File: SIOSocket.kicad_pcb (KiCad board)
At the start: 2 copper layers, 46 x 26 mm, 3 parts, among them J1 Atari_SIO_Connector, J2 Conn_2Rows-13Pins

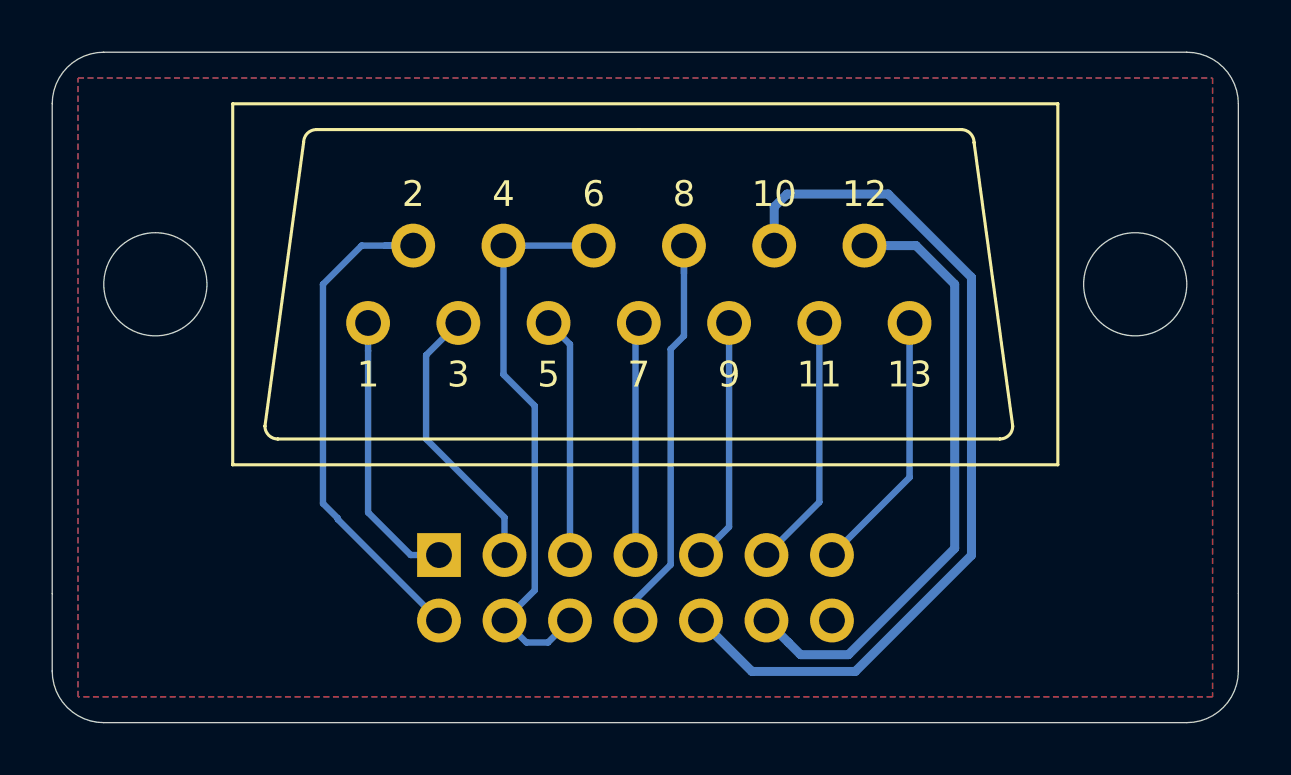
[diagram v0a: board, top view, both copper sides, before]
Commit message: Upgrade to KiCad 5.1 and changes to 3D printed SIO port for Atari800XL PCB Project
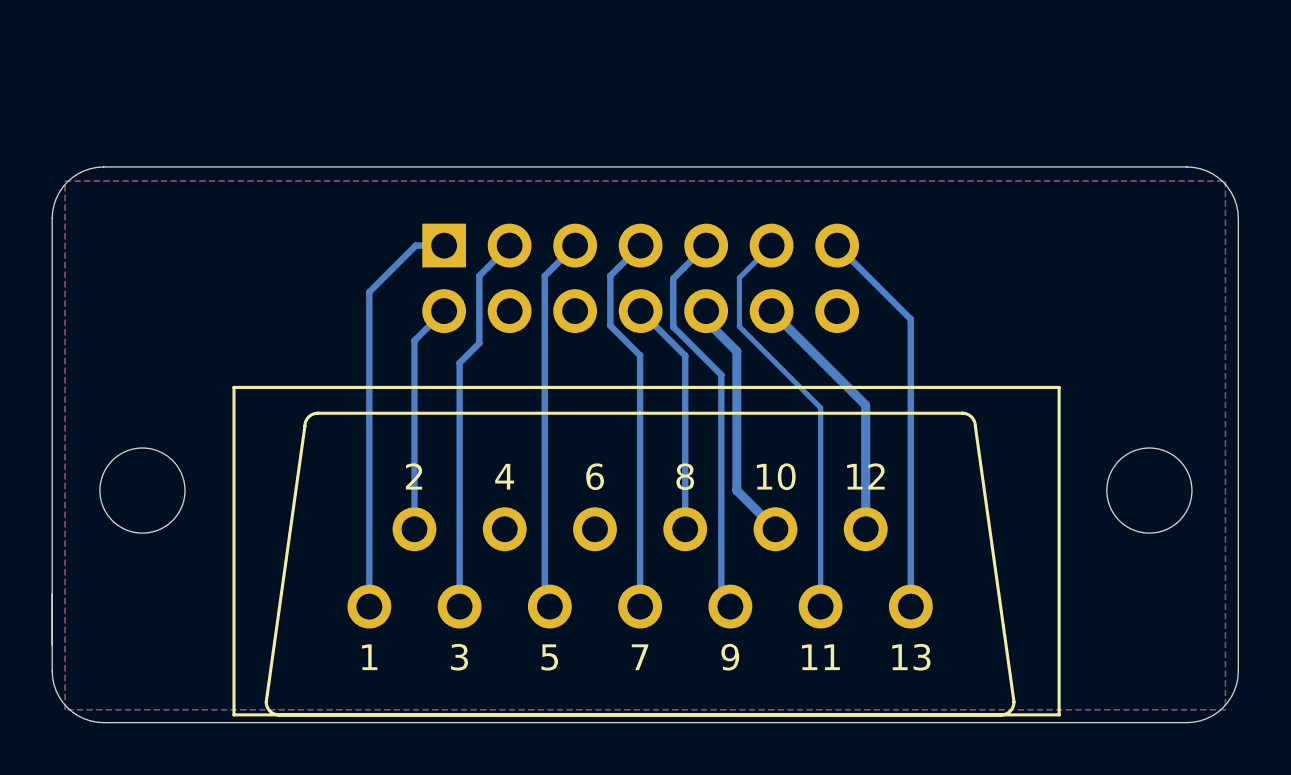
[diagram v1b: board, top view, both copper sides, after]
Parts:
- moved J2 12.0 mm to (140.2, 86.5)
- moved REF** 11.3 mm to (131.7, 87.7)
- moved J1 11.0 mm to (146.1, 105.0)
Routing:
- net +5V: track 34.6 -> 9.57 mm
- net GND: track 22.3 -> 0.00 mm
- net +12V: track 23.9 -> 9.97 mm
- net Net-(J1-Pad2): track 20.1 -> 8.94 mm
- net Net-(J1-Pad8): track 16.4 -> 9.18 mm
- net Net-(J1-Pad11): track 9.85 -> 15.9 mm
- net Net-(J1-Pad9): track 9.45 -> 15.4 mm
- net Net-(J1-Pad7): track 9.05 -> 15.0 mm
- net Net-(J1-Pad5): track 9.34 -> 14.6 mm
- net Net-(J1-Pad1): track 10.8 -> 15.8 mm
- net Net-(J1-Pad13): track 10.2 -> 15.2 mm
- net Net-(J1-Pad3): track 10.8 -> 14.8 mm
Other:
- board size 46 x 26 mm -> 46 x 21.5 mm
- board text added: "ATARI SIO Connector v2.0 Paweł Mandes 2019 Marek Łyczba 2020 Creative Commons BY-SA"
- board text removed: "ATARI SIO Connector v1.0 Paweł Mandes 2019 Creative Commons BY-SA"
